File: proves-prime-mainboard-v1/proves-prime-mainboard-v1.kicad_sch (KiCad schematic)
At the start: 30 parts, among them IC1 RP2040_QFN56, IC2 AZ1117CH-3.3TRG1, U1 W25Q128JV, Y1 12MHZ

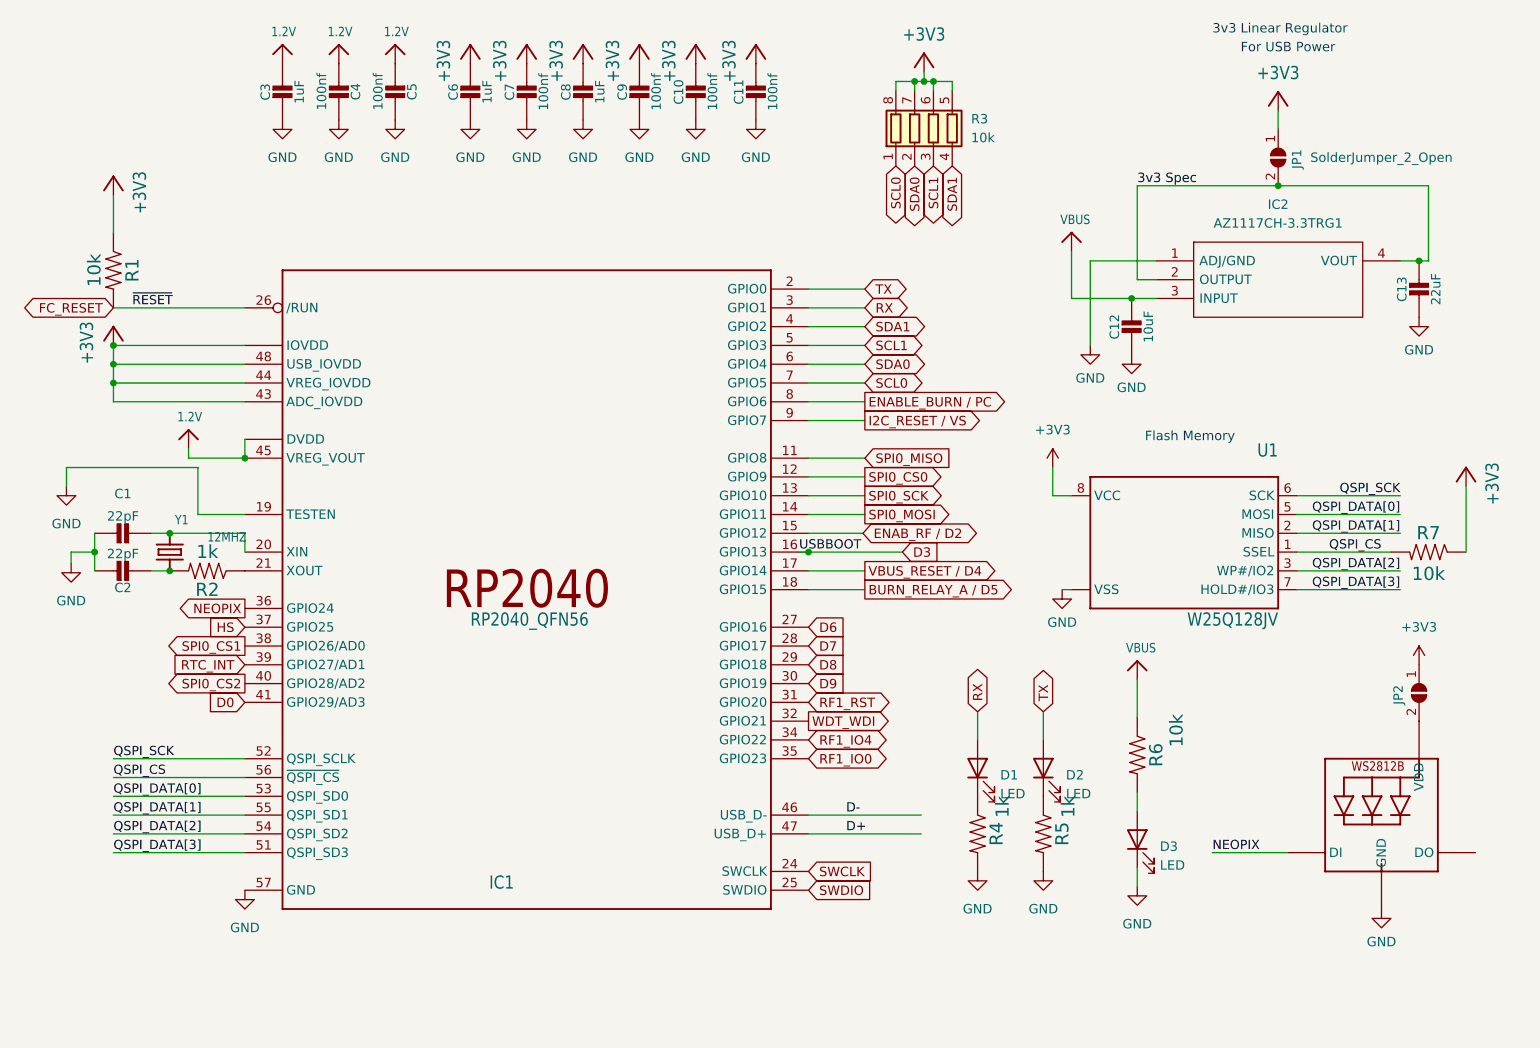
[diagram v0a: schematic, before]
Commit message: Set Up Hierarchical Sheets
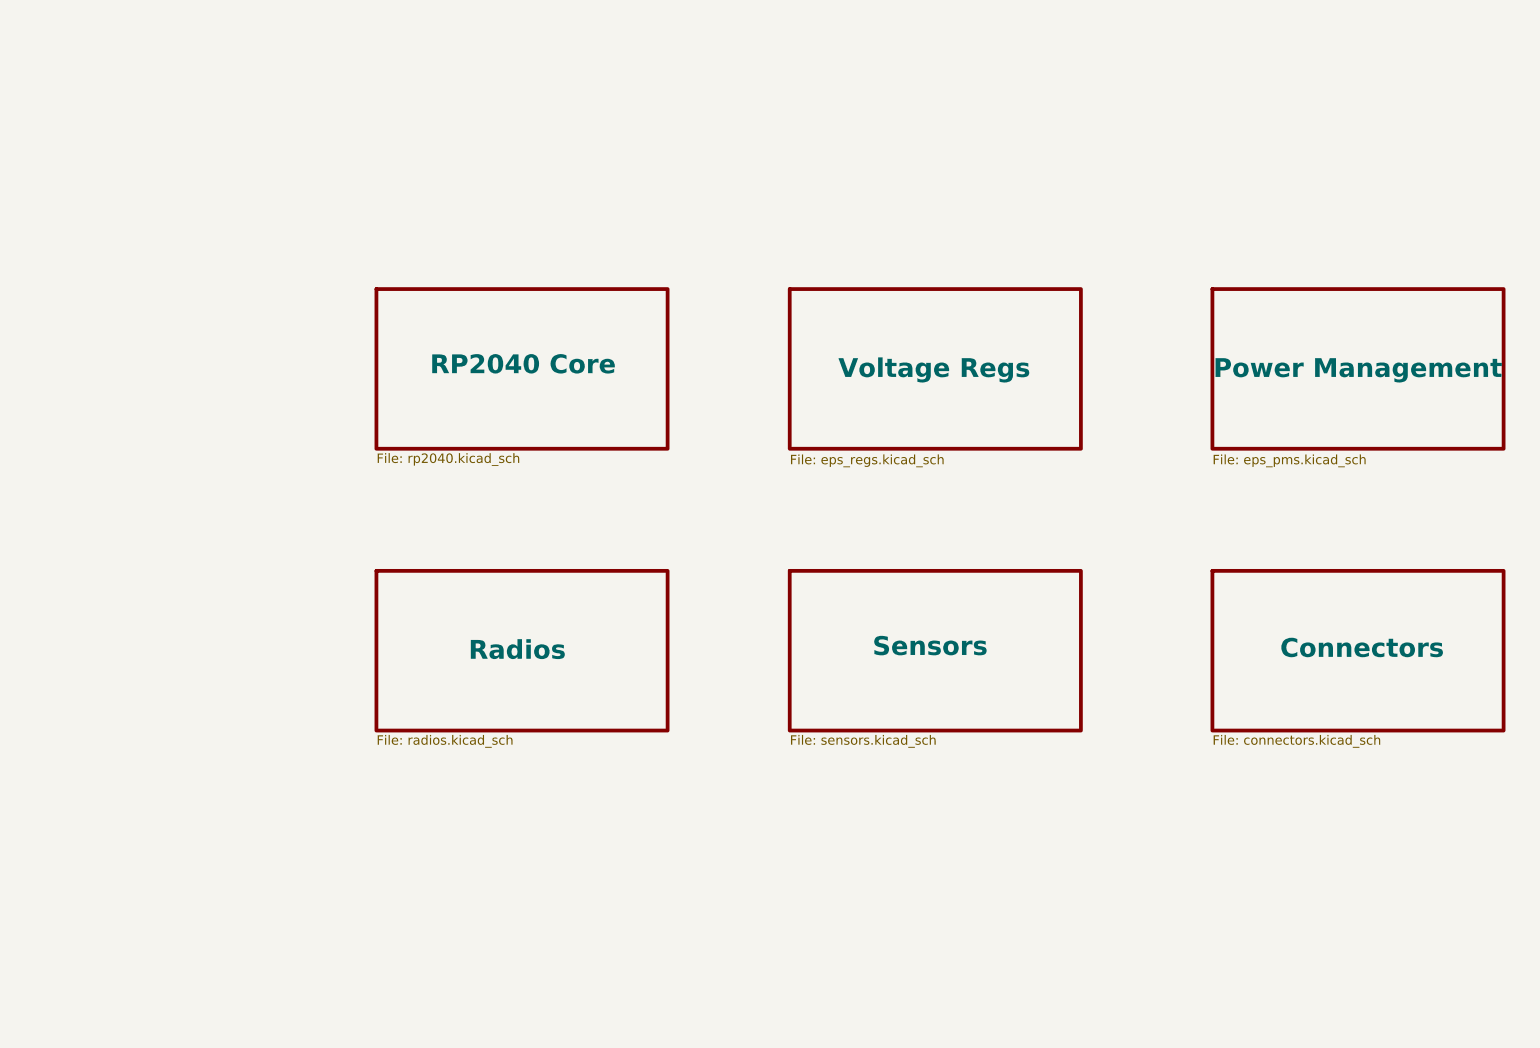
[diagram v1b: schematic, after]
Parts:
- removed C1, C2: 22pF, Capacitor_SMD:C_0402_1005Metric, symbol Adafruit ItsyBitsy RP2040-eagle-import:CAP_CERAMIC_0402NO
- removed C10, C11, C4, C5, C7, C9: 100nf, Capacitor_SMD:C_0402_1005Metric, symbol Adafruit ItsyBitsy RP2040-eagle-import:CAP_CERAMIC_0402NO
- removed C12: 10uF, Capacitor_SMD:C_0603_1608Metric, symbol Adafruit ItsyBitsy RP2040-eagle-import:CAP_CERAMIC_0603MP
- removed C13: 22uF, Capacitor_SMD:C_0603_1608Metric, symbol Adafruit ItsyBitsy RP2040-eagle-import:CAP_CERAMIC_0603MP
- removed C3, C6, C8: 1uF, Capacitor_SMD:C_0603_1608Metric, symbol Adafruit ItsyBitsy RP2040-eagle-import:CAP_CERAMIC_0603MP
- removed D1, D2, D3: LED, LED_SMD:LED_0603_1608Metric, symbol Device:LED
- removed IC1: RP2040_QFN56, Package_DFN_QFN:QFN-56-1EP_7x7mm_P0.4mm_EP3.2x3.2mm_ThermalVias, symbol Adafruit ItsyBitsy RP2040-eagle-import:RP2040_QFN56
- removed IC2: AZ1117CH-3.3TRG1, Package_TO_SOT_SMD:SOT-223, symbol AZ1117CH-3.3TRG1:AZ1117CH-3.3TRG1
- removed JP1, JP2: SolderJumper_2_Open, Jumper:SolderJumper-2_P1.3mm_Open_RoundedPad1.0x1.5mm, symbol Jumper:SolderJumper_2_Open
- removed LED1: WS2812B_SK6812_1515, LED_SMD:LED_WS2812B_PLCC4_5.0x5.0mm_P3.2mm, symbol Adafruit ItsyBitsy RP2040-eagle-import:WS2812B_SK6805_1515
- removed R1, R6, R7: 10k, Resistor_SMD:R_0603_1608Metric, symbol mainboard:RESISTOR0603
- removed R2: 1k, Resistor_SMD:R_0402_1005Metric, symbol mainboard:RESISTOR0603
- removed R3: 10k, Resistor_SMD:R_Array_Convex_4x0603, symbol Device:R_Pack04
- removed R4, R5: 1k, Resistor_SMD:R_0603_1608Metric, symbol mainboard:RESISTOR0603
- removed U1: W25Q128JV, Package_SO:SOIC-8_5.275x5.275mm_P1.27mm, symbol Adafruit ItsyBitsy RP2040-eagle-import:SPIFLASH_8PIN_4X4
- removed Y1: 12MHZ, Crystal:Crystal_SMD_2520-4Pin_2.5x2.0mm, symbol Adafruit ItsyBitsy RP2040-eagle-import:CRYSTAL2.5X2.0
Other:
- added sheet  Power Management (eps_pms.kicad_sch)
- added sheet Connectors (connectors.kicad_sch)
- added sheet RP2040 Core (rp2040.kicad_sch)
- added sheet Radios (radios.kicad_sch)
- added sheet Sensors (sensors.kicad_sch)
- added sheet Voltage Regs (eps_regs.kicad_sch)
- note removed: "3v3 Linear Regulator"
- note removed: "Flash Memory"
- note removed: "For USB Power"

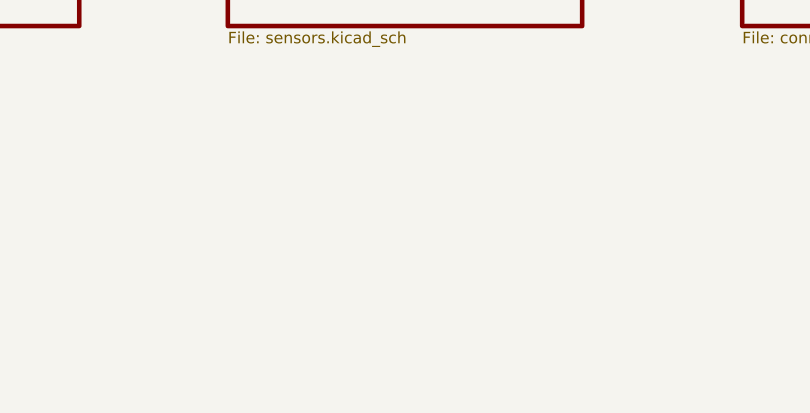
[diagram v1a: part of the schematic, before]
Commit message: Copied Watchdog Circuit
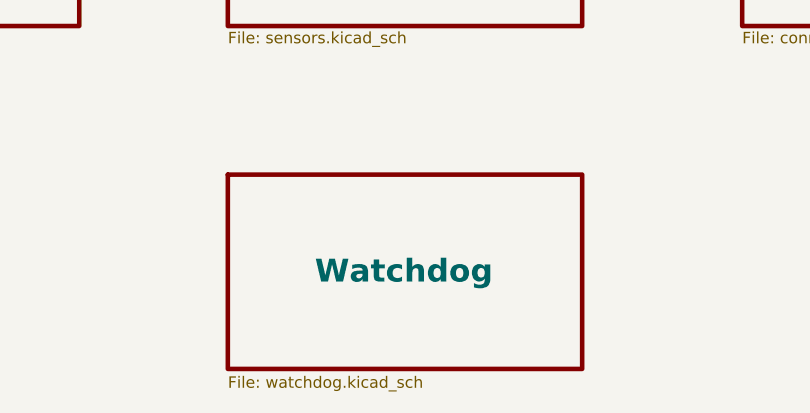
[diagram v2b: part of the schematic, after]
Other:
- added sheet Watchdog (watchdog.kicad_sch)
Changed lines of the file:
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@@
+	)
+	(sheet
+		(at 127 139.7)
+		(size 39.37 21.59)
+		(stroke
+			(width 0.508)
+			(type solid)
+			(color 0 0 0 1)
+		)
+		(fill
+			(color 88 255 116 1.0000)
+		)
+		(property "Sheetname" "Watchdog"
+			(at 146.558 151.892 0)
+			(effects
+				(font
+					(face "Courier New")
+					(size 2.54 2.54)
+					(bold yes)
+					(color 0 0 0 1)
+				)
+				(justify bottom)
+			)
+		)
+		(property "Sheetfile" "watchdog.kicad_sch"
+			(at 127 162.0524 0)
+			(effects
+				(font
+					(size 1.27 1.27)
+				)
+				(justify left top)
+			)
+		)
+		(instances
+			(project "proves-prime-mainboard-v1"
+				(path "/6cfe8c53-6734-42c5-b115-bce78073d1a6"
+					(page "8")
+				)
+			)
+		)
 	)
 	(sheet

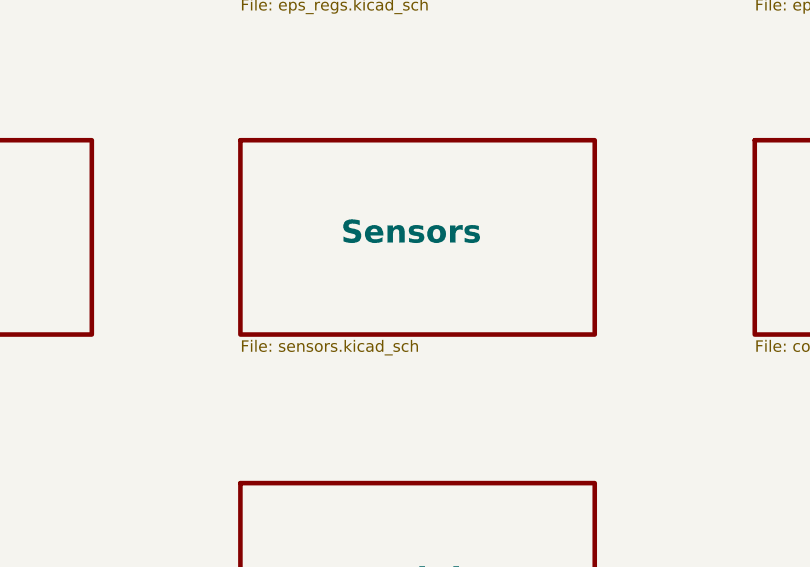
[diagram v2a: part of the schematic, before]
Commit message: Migrated FC Board Elements
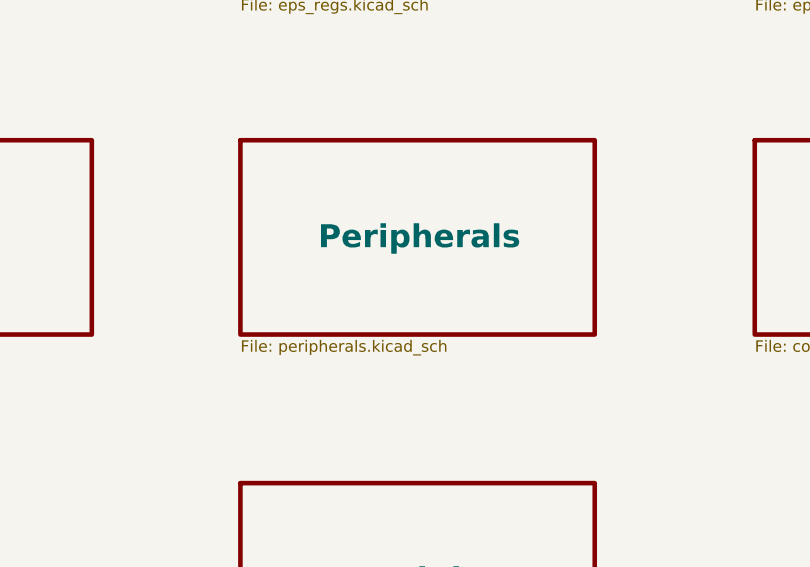
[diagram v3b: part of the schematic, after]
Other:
- sheet Sensors renamed Peripherals
- sheet Peripherals: file sensors.kicad_sch -> peripherals.kicad_sch
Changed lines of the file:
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@@
 			(color 162 18 255 1.0000)
 		)
-		(property "Sheetname" "Sensors"
-			(at 138.176 113.284 0)
+		(property "Sheetname" "Peripherals"
+			(at 135.636 113.792 0)
 			(effects
 				(font
@@
 			)
 		)
-		(property "Sheetfile" "sensors.kicad_sch"
+		(property "Sheetfile" "peripherals.kicad_sch"
 			(at 127 123.7746 0)
 			(effects

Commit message: Migrated Temperature Sensor
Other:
- added sheet Burnwire & Heater (burn_heat.kicad_sch)
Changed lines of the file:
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@@
 	(paper "A4")
 	(sheet
-		(at 71.12 101.6)
+		(at 71.12 82.55)
 		(size 39.37 21.59)
 		(stroke
@@
 		)
 		(property "Sheetname" "Radios"
-			(at 83.566 113.792 0)
+			(at 83.566 94.742 0)
 			(effects
 				(font
@@
 		)
 		(property "Sheetfile" "radios.kicad_sch"
-			(at 71.12 123.7746 0)
+			(at 71.12 104.7246 0)
 			(effects
 				(font
@@
 	)
 	(sheet
-		(at 184.15 101.6)
+		(at 184.15 82.55)
 		(size 39.37 21.59)
 		(stroke
@@
 		)
 		(property "Sheetname" "Connectors"
-			(at 193.294 113.538 0)
+			(at 193.294 94.488 0)
 			(effects
 				(font
@@
 		)
 		(property "Sheetfile" "connectors.kicad_sch"
-			(at 184.15 123.7746 0)
+			(at 184.15 104.7246 0)
 			(effects
 				(font
@@
 	)
 	(sheet
-		(at 127 63.5)
+		(at 127 44.45)
 		(size 39.37 21.59)
 		(stroke
@@
 		)
 		(property "Sheetname" "Voltage Regs"
-			(at 146.558 75.692 0)
+			(at 146.558 56.642 0)
 			(effects
 				(font
@@
 		)
 		(property "Sheetfile" "eps_regs.kicad_sch"
-			(at 127 85.8524 0)
+			(at 127 66.8024 0)
 			(effects
 				(font
@@
 	)
 	(sheet
-		(at 184.15 63.5)
+		(at 184.15 44.45)
 		(size 39.37 21.59)
 		(stroke
@@
 		)
 		(property "Sheetname" " Power Management"
-			(at 203.2 75.692 0)
+			(at 203.2 56.642 0)
 			(effects
 				(font
@@
 		)
 		(property "Sheetfile" "eps_pms.kicad_sch"
-			(at 184.15 85.8524 0)
+			(at 184.15 66.8024 0)
 			(effects
 				(font
@@
 	)
 	(sheet
-		(at 71.12 63.5)
+		(at 71.12 44.45)
 		(size 39.37 21.59)
 		(stroke
@@
 		)
 		(property "Sheetname" "RP2040 Core"
-			(at 90.932 75.184 0)
+			(at 90.932 56.134 0)
 			(effects
 				(font
@@
 		)
 		(property "Sheetfile" "rp2040.kicad_sch"
-			(at 71.12 85.6746 0)
+			(at 71.12 66.6246 0)
 			(effects
 				(font
@@
 	)
 	(sheet
-		(at 127 139.7)
+		(at 100.33 119.38)
 		(size 39.37 21.59)
 		(stroke
@@
 		)
 		(property "Sheetname" "Watchdog"
-			(at 146.558 151.892 0)
+			(at 119.888 131.572 0)
 			(effects
 				(font
@@
 		)
 		(property "Sheetfile" "watchdog.kicad_sch"
-			(at 127 162.0524 0)
+			(at 100.33 141.7324 0)
 			(effects
 				(font
@@
 	)
 	(sheet
-		(at 127 101.6)
+		(at 156.21 119.38)
+		(size 39.37 21.59)
+		(stroke
+			(width 0.508)
+			(type solid)
+			(color 0 0 0 1)
+		)
+		(fill
+			(color 255 39 228 1.0000)
+		)
+		(property "Sheetname" "Burnwire & Heater"
+			(at 175.768 131.572 0)
+			(effects
+				(font
+					(face "Courier New")
+					(size 2.54 2.54)
+					(bold yes)
+					(color 0 0 0 1)
+				)
+				(justify bottom)
+			)
+		)
+		(property "Sheetfile" "burn_heat.kicad_sch"
+			(at 156.21 141.7324 0)
+			(effects
+				(font
+					(size 1.27 1.27)
+				)
+				(justify left top)
+			)
+		)
+		(instances
+			(project "proves-prime-mainboard-v1"
+				(path "/6cfe8c53-6734-42c5-b115-bce78073d1a6"
+					(page "10")
+				)
+			)
+		)
+	)
+	(sheet
+		(at 127 82.55)
 		(size 39.37 21.59)
 		(stroke
@@
 		)
 		(property "Sheetname" "Peripherals"
-			(at 135.636 113.792 0)
+			(at 135.636 94.742 0)
 			(effects
 				(font
@@
 		)
 		(property "Sheetfile" "peripherals.kicad_sch"
-			(at 127 123.7746 0)
-			(effects
-				(font
+			(at 127 104.7246 0)
+			(effects
+				(font

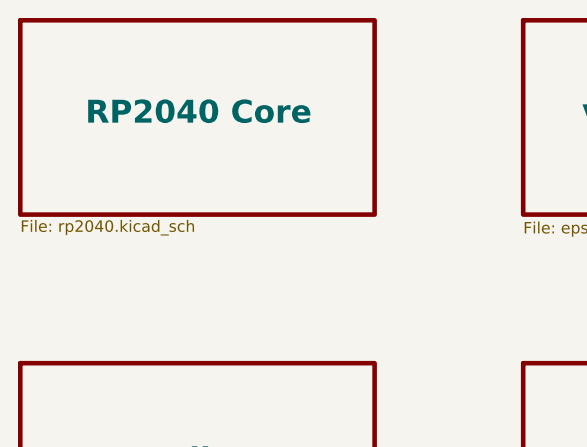
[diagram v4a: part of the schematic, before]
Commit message: Added PGA2350 Library
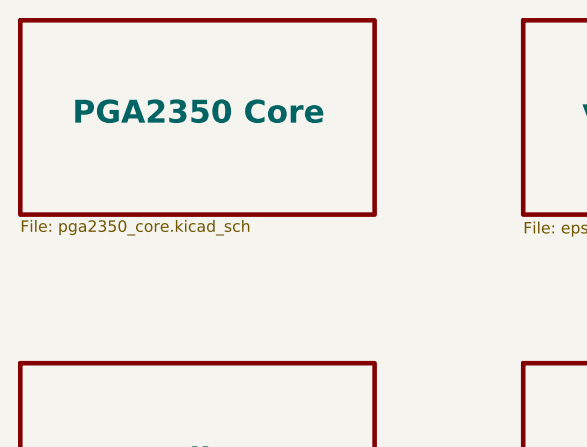
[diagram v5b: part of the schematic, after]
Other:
- sheet RP2040 Core renamed PGA2350 Core
- sheet PGA2350 Core: file rp2040.kicad_sch -> pga2350_core.kicad_sch
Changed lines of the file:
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@@
 			(color 0 249 255 1.0000)
 		)
-		(property "Sheetname" "RP2040 Core"
+		(property "Sheetname" "PGA2350 Core"
 			(at 90.932 56.134 0)
 			(effects
@@
 			)
 		)
-		(property "Sheetfile" "rp2040.kicad_sch"
+		(property "Sheetfile" "pga2350_core.kicad_sch"
 			(at 71.12 66.6246 0)
 			(effects

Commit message: Created MVS Sheet
Minimum Viable Satellite
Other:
- added sheet Minimum Viable (mvs.kicad_sch)
- note added: "Satellite"
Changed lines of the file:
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@@
 	(generator_version "8.0")
 	(paper "A4")
-	(sheet
-		(at 71.12 82.55)
+	(text "Satellite"
+		(exclude_from_sim no)
+		(at 146.05 40.894 0)
+		(effects
+			(font
+				(face "Courier New")
+				(size 2.54 2.54)
+				(thickness 0.508)
+				(bold yes)
+				(color 0 0 0 1)
+			)
+		)
+	)
+	(sheet
+		(at 71.12 95.25)
 		(size 39.37 21.59)
 		(stroke
@@
 		)
 		(property "Sheetname" "Radios"
-			(at 83.566 94.742 0)
+			(at 83.566 107.442 0)
 			(effects
 				(font
@@
 		)
 		(property "Sheetfile" "radios.kicad_sch"
-			(at 71.12 104.7246 0)
+			(at 71.12 117.4246 0)
 			(effects
 				(font
@@
 	)
 	(sheet
-		(at 184.15 82.55)
+		(at 184.15 95.25)
 		(size 39.37 21.59)
 		(stroke
@@
 		)
 		(property "Sheetname" "Connectors"
-			(at 193.294 94.488 0)
+			(at 193.294 107.188 0)
 			(effects
 				(font
@@
 		)
 		(property "Sheetfile" "connectors.kicad_sch"
-			(at 184.15 104.7246 0)
+			(at 184.15 117.4246 0)
 			(effects
 				(font
@@
 	)
 	(sheet
-		(at 127 44.45)
+		(at 127 57.15)
 		(size 39.37 21.59)
 		(stroke
@@
 		)
 		(property "Sheetname" "Voltage Regs"
-			(at 146.558 56.642 0)
+			(at 146.558 69.342 0)
 			(effects
 				(font
@@
 		)
 		(property "Sheetfile" "eps_regs.kicad_sch"
-			(at 127 66.8024 0)
+			(at 127 79.5024 0)
 			(effects
 				(font
@@
 	)
 	(sheet
-		(at 184.15 44.45)
+		(at 184.15 57.15)
 		(size 39.37 21.59)
 		(stroke
@@
 		)
 		(property "Sheetname" " Power Management"
-			(at 203.2 56.642 0)
+			(at 203.2 69.342 0)
 			(effects
 				(font
@@
 		)
 		(property "Sheetfile" "eps_pms.kicad_sch"
-			(at 184.15 66.8024 0)
+			(at 184.15 79.5024 0)
 			(effects
 				(font
@@
 	)
 	(sheet
-		(at 71.12 44.45)
+		(at 127 26.67)
+		(size 39.37 21.59)
+		(stroke
+			(width 0.508)
+			(type solid)
+			(color 0 0 0 1)
+		)
+		(fill
+			(color 99 164 255 1.0000)
+		)
+		(property "Sheetname" "Minimum Viable"
+			(at 147.32 35.56 0)
+			(effects
+				(font
+					(face "Courier New")
+					(size 2.54 2.54)
+					(bold yes)
+					(color 0 0 0 0.7)
+				)
+				(justify bottom)
+			)
+		)
+		(property "Sheetfile" "mvs.kicad_sch"
+			(at 127 49.0224 0)
+			(effects
+				(font
+					(size 1.27 1.27)
+				)
+				(justify left top)
+			)
+		)
+		(instances
+			(project "proves-prime-mainboard-v1"
+				(path "/6cfe8c53-6734-42c5-b115-bce78073d1a6"
+					(page "11")
+				)
+			)
+		)
+	)
+	(sheet
+		(at 71.12 57.15)
 		(size 39.37 21.59)
 		(stroke
@@
 		)
 		(property "Sheetname" "PGA2350 Core"
-			(at 90.932 56.134 0)
+			(at 90.932 68.834 0)
 			(effects
 				(font
@@
 		)
 		(property "Sheetfile" "pga2350_core.kicad_sch"
-			(at 71.12 66.6246 0)
+			(at 71.12 79.3246 0)
 			(effects
 				(font
@@
 	)
 	(sheet
-		(at 100.33 119.38)
+		(at 100.33 132.08)
 		(size 39.37 21.59)
 		(stroke
@@
 		)
 		(property "Sheetname" "Watchdog"
-			(at 119.888 131.572 0)
+			(at 119.888 144.272 0)
 			(effects
 				(font
@@
 		)
 		(property "Sheetfile" "watchdog.kicad_sch"
-			(at 100.33 141.7324 0)
+			(at 100.33 154.4324 0)
 			(effects
 				(font
@@
 	)
 	(sheet
-		(at 156.21 119.38)
+		(at 156.21 132.08)
 		(size 39.37 21.59)
 		(stroke
@@
 		)
 		(property "Sheetname" "Burnwire & Heater"
-			(at 175.768 131.572 0)
+			(at 175.768 144.272 0)
 			(effects
 				(font
@@
 		)
 		(property "Sheetfile" "burn_heat.kicad_sch"
-			(at 156.21 141.7324 0)
+			(at 156.21 154.4324 0)
 			(effects
 				(font
@@
 	)
 	(sheet
-		(at 127 82.55)
+		(at 127 95.25)
 		(size 39.37 21.59)
 		(stroke
@@
 		)
 		(property "Sheetname" "Peripherals"
-			(at 135.636 94.742 0)
+			(at 135.636 107.442 0)
 			(effects
 				(font
@@
 		)
 		(property "Sheetfile" "peripherals.kicad_sch"
-			(at 127 104.7246 0)
-			(effects
-				(font
+			(at 127 117.4246 0)
+			(effects
+				(font
